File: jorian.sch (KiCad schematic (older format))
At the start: 56 parts, among them J1 Conn_01x08

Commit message: second commit
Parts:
- removed J1: Conn_01x08, kbd:connector_custom_small, symbol Connector_Generic:Conn_01x08
- added G1, G2: Logo_Open_Hardware_Small, kbd:jorian_logo, symbol Graphic:Logo_Open_Hardware_Small
- added H1: Battery Pad, kbd:battery_pad, symbol Mechanical:MountingHole_Pad
- added J2: conn_i2c, kbd:connector_i2c, symbol Connector_Generic:Conn_01x04
- added J3: conn_swd, kbd:connector_swd, symbol Connector_Generic:Conn_01x05
- added JP1: BAT+, kbd:jumper_3way, symbol Jumper:SolderJumper_3_Open
- added JP2: GND, kbd:jumper_3way, symbol Jumper:SolderJumper_3_Open
- added JP3: VCC, kbd:jumper_3way, symbol Jumper:SolderJumper_3_Open
- added JP4: SCL, kbd:jumper_3way, symbol Jumper:SolderJumper_3_Open
- added JP5: SDA, kbd:jumper_3way, symbol Jumper:SolderJumper_3_Open
- BT1: value Battery_Cell -> Battery Holder
- E10, E15, E18, E5: value edge_conn_left -> left; symbol kbd:edge_conn -> Connector_Generic:Conn_01x05
- E16, E19, E20, E21: value edge_conn_right -> right; symbol kbd:edge_conn -> Connector_Generic:Conn_01x05
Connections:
- net labels added: RX, SWC, SWD, TX
- net labels removed: SWCLK, SWDIO
- wire segments 264 -> 275
- no-connect marks 7 -> 17
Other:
- moved on the sheet: BT1

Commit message: added charger
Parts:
- removed J2: conn_i2c, kbd:connector_i2c, symbol Connector_Generic:Conn_01x04
- removed J3: conn_swd, kbd:connector_swd, symbol Connector_Generic:Conn_01x05
- removed JP1: BAT+, kbd:jumper_3way, symbol Jumper:SolderJumper_3_Open
- removed JP2: GND, kbd:jumper_3way, symbol Jumper:SolderJumper_3_Open
- removed JP3: VCC, kbd:jumper_3way, symbol Jumper:SolderJumper_3_Open
- removed JP4: SCL, kbd:jumper_3way, symbol Jumper:SolderJumper_3_Open
- removed JP5: SDA, kbd:jumper_3way, symbol Jumper:SolderJumper_3_Open
- added C3, C4: 0.1uF, kbd:C_0805, symbol Device:C
- added C5: 10uF, kbd:C_0805, symbol Device:C
- added J1, J3: MicroUSB, kbd:usb_micro_custom, symbol Connector:USB_B_Micro
- added J2, J4: USB-C, kbd:usb_type_c, symbol Connector:USB_C_Receptacle_USB2.0
- added J5: MJ-4PP-9, kbd:trrs_connector, symbol kbd:kbd_MJ-4PP-9
- added JP1: B+, kbd:jumper, symbol Device:Jumper_NO_Small
- added JP10: B-, kbd:jumper, symbol Device:Jumper_NO_Small
- added JP11, JP13: VCC, kbd:jumper, symbol Device:Jumper_NO_Small
- added JP12, JP14: GND, kbd:jumper, symbol Device:Jumper_NO_Small
- added JP15: SKIP, kbd:jumper, symbol Device:Jumper_NO_Small
- added JP2, JP3, JP4, JP5, JP6, JP7, JP8, JP9: (no value), kbd:jumper, symbol Device:Jumper_NO_Small
- added OLED1, OLED2: I2C_conn, kbd:connector_i2c, symbol Connector_Generic:Conn_01x04
- added R1: 1.2K, kbd:R_0805, symbol Device:R
- added R2: 1K, kbd:R_0805, symbol Device:R
- added R3: 100, kbd:R_0805, symbol Device:R
- added SW1: SW_SPDT, kbd:switch_MSK-12C02_smd, symbol Switch:SW_SPDT
- added SWD1: SWD_conn, kbd:connector_swd, symbol Connector_Generic:Conn_01x05
- added U3: AMS1117, kbd:SOT-223-3, symbol Regulator_Linear:AMS1117
- added U4: TP4056, kbd:SOP-8, symbol kbd:TP4056
- added U5: DW01A, kbd:SOT-23-6, symbol kbd:DW01A
- added U6: FS8205A, kbd:TSSOP-8, symbol kbd:FS8205A
- E10, E15, E18, E5: footprint kbd:edge_conn_left -> kbd:edge_conn; symbol Connector_Generic:Conn_01x05 -> Connector_Generic:Conn_01x04
- E16, E19, E20, E21: footprint kbd:edge_conn_right -> kbd:edge_conn; symbol Connector_Generic:Conn_01x05 -> Connector_Generic:Conn_01x04
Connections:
- net labels added: 3.3V, 5V, B+, B-, BAT+, D+, D-, IN+, IN-, OUT+, OUT-
- wire segments 275 -> 372
- no-connect marks 17 -> 26
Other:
- note added: "LiPo Charger"
- moved on the sheet: H1

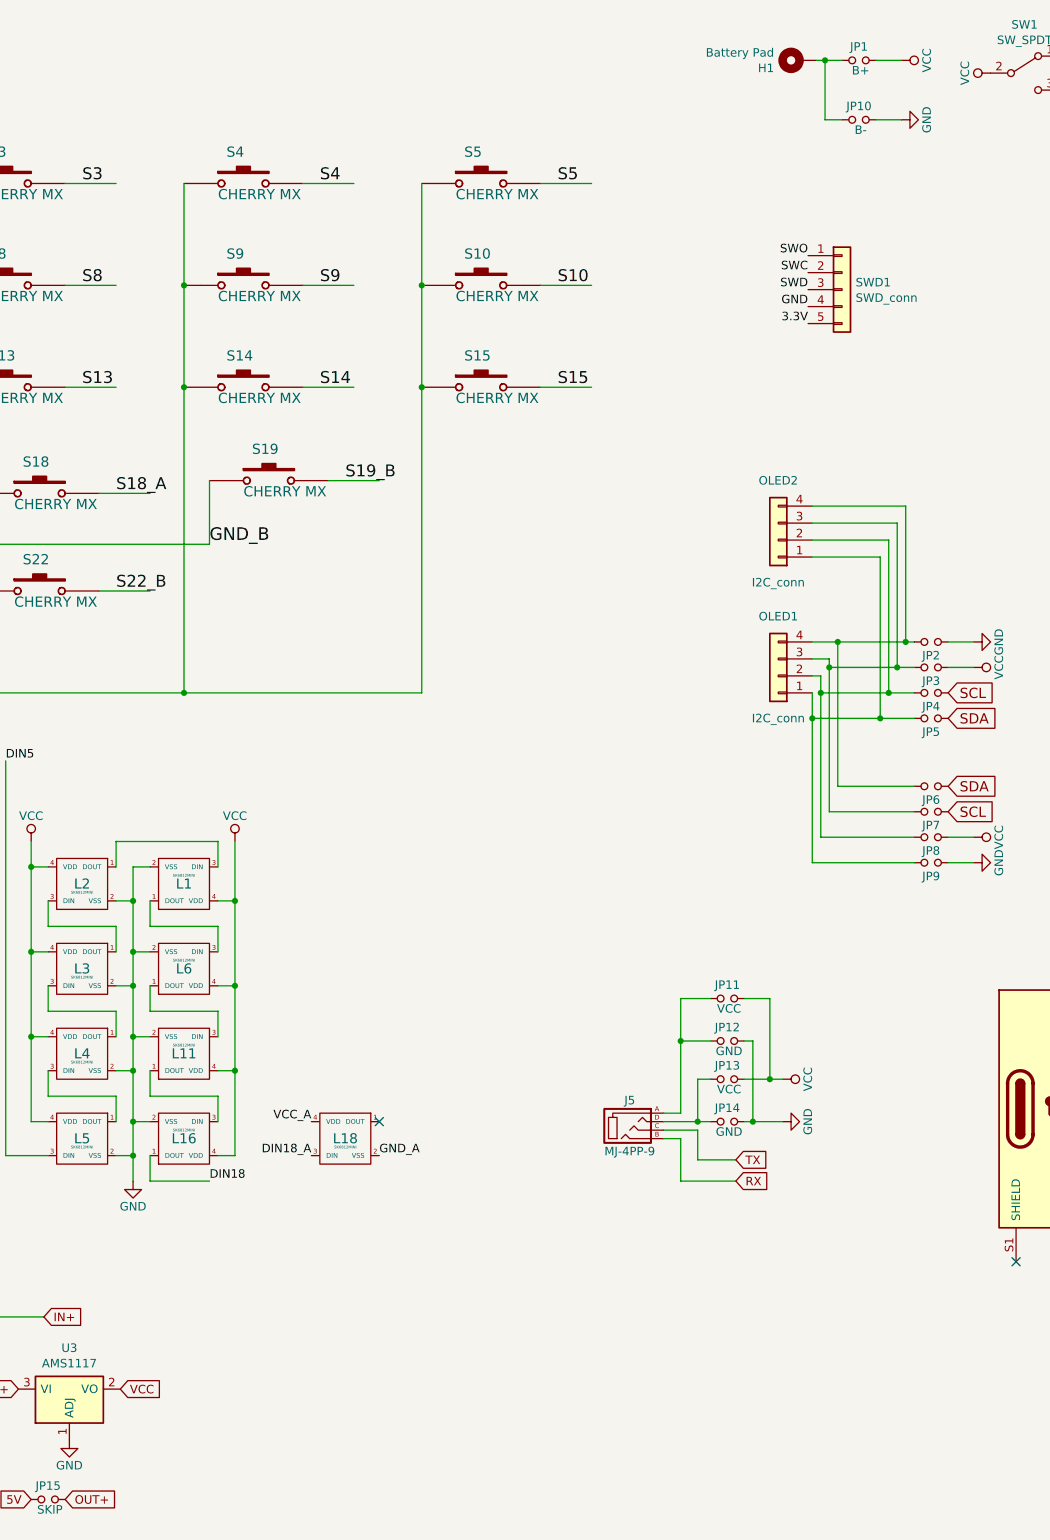
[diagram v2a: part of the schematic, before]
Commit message: autorouted charger take 1
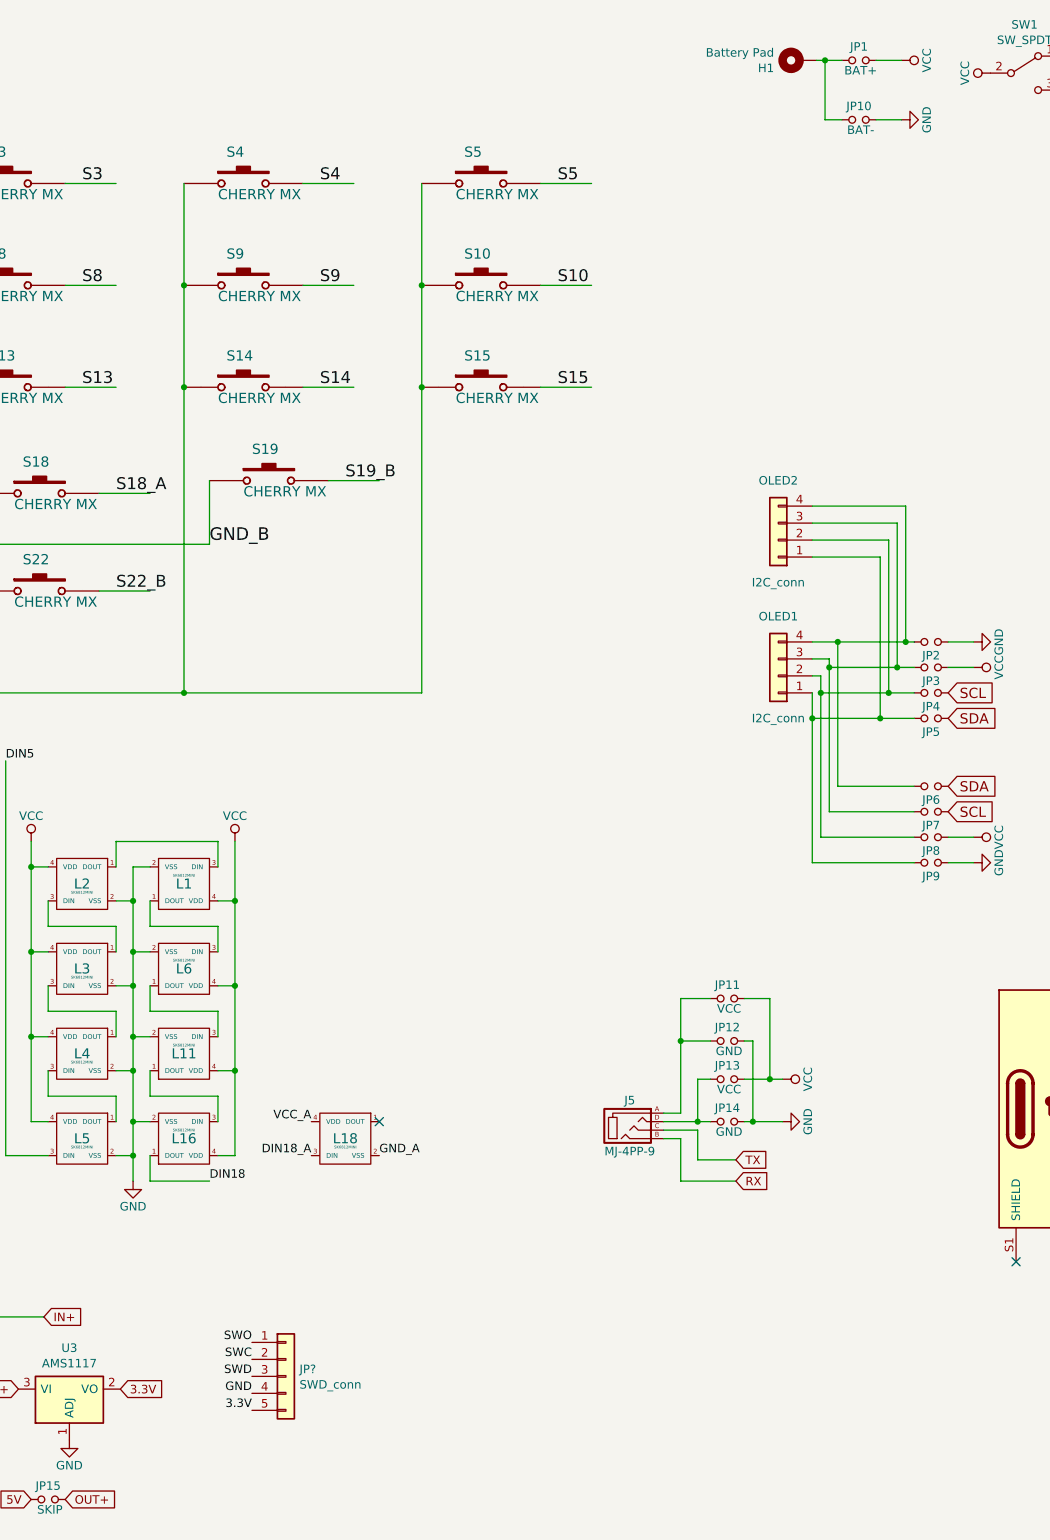
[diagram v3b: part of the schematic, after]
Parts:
- JP1: value B+ -> BAT+
- JP10: value B- -> BAT-
- renumbered SWD1 to JP?
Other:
- moved on the sheet: JP?
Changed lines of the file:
@@
 	1    0    0    -1
 $EndComp
-Text Label 12575 2175 2    50   ~ 0
+Text Label 9300 8575 2    50   ~ 0
 SWO
-Text Label 12575 2275 2    50   ~ 0
+Text Label 9300 8675 2    50   ~ 0
 SWC
-Text Label 12575 2375 2    50   ~ 0
+Text Label 9300 8775 2    50   ~ 0
 SWD
-Text Label 12575 2475 2    50   ~ 0
+Text Label 9300 8875 2    50   ~ 0
 GND
-Text Label 12575 2575 2    50   ~ 0
+Text Label 9300 8975 2    50   ~ 0
 3.3V
 Text Label 14050 1200 0    50   ~ 0
@@
 	12750 4450 13150 4450
 $Comp
-L Connector_Generic:Conn_01x05 SWD1
+L Connector_Generic:Conn_01x05 JP?
 U 1 1 5C1CF656
-P 12775 2375
-F 0 "SWD1" H 12855 2417 50  0000 L CNN
-F 1 "SWD_conn" H 12855 2326 50  0000 L CNN
-F 2 "kbd:connector_swd" H 12775 2375 50  0001 C CNN
-F 3 "~" H 12775 2375 50  0001 C CNN
-	1    12775 2375
+P 9500 8775
+F 0 "JP?" H 9580 8817 50  0000 L CNN
+F 1 "SWD_conn" H 9580 8726 50  0000 L CNN
+F 2 "kbd:connector_swd" H 9500 8775 50  0001 C CNN
+F 3 "~" H 9500 8775 50  0001 C CNN
+	1    9500 8775
 	1    0    0    -1
 $EndComp
@@
 P 12875 1025
 F 0 "JP1" H 12875 1105 50  0000 C CNN
-F 1 "B+" H 12885 965 50  0000 C CNN
+F 1 "BAT+" H 12885 965 50  0000 C CNN
 F 2 "kbd:jumper" H 12875 1025 50  0001 C CNN
 F 3 "" H 12875 1025 50  0001 C CNN
@@
 P 12875 1375
 F 0 "JP10" H 12875 1455 50  0000 C CNN
-F 1 "B-" H 12885 1315 50  0000 C CNN
+F 1 "BAT-" H 12885 1315 50  0000 C CNN
 F 2 "kbd:jumper" H 12875 1375 50  0001 C CNN
 F 3 "" H 12875 1375 50  0001 C CNN
@@
 5V
 Text GLabel 8525 8850 2    50   Input ~ 0
-VCC
+3.3V
 Text GLabel 7800 8425 0    50   Input ~ 0
 5V

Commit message: autorouted charger take 2
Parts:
- JP1: value BAT+ -> B+
- JP10: value BAT- -> B-
- gave numbers to parts that had none: 1
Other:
- moved on the sheet: BT1, H1, JP1, JP10, JP15, JP16, SW1
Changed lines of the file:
@@
 L Device:Battery_Cell BT1
 U 1 1 5C194810
-P 14725 1075
-F 0 "BT1" H 14843 1171 50  0000 L CNN
-F 1 "Battery Holder" H 14843 1080 50  0000 L CNN
-F 2 "kbd:cr2032_bs-7" V 14725 1135 50  0001 C CNN
-F 3 "~" V 14725 1135 50  0001 C CNN
-	1    14725 1075
+P 9400 8850
+F 0 "BT1" H 9518 8946 50  0000 L CNN
+F 1 "Battery Holder" H 9518 8855 50  0000 L CNN
+F 2 "kbd:cr2032_bs-7" V 9400 8910 50  0001 C CNN
+F 3 "~" V 9400 8910 50  0001 C CNN
+	1    9400 8850
 	1    0    0    -1
 $EndComp
@@
 Wire Wire Line
 	2850 2300 3150 2300
-Text Label 14725 875  0    50   ~ 0
+Text Label 9400 8650 0    50   ~ 0
 BAT+
-Text Label 14725 1175 0    50   ~ 0
+Text Label 9400 8950 0    50   ~ 0
 GND
 Text Label 1250 1300 2    70   ~ 0
@@
 L Mechanical:MountingHole_Pad H1
 U 1 1 5C36F98B
-P 12525 1025
-F 0 "H1" V 12479 1175 50  0000 L CNN
-F 1 "Battery Pad" V 12570 1175 50  0000 L CNN
-F 2 "kbd:battery_pad" H 12525 1025 50  0001 C CNN
-F 3 "~" H 12525 1025 50  0001 C CNN
-	1    12525 1025
+P 9725 9400
+F 0 "H1" V 9679 9550 50  0000 L CNN
+F 1 "Battery Pad" V 9770 9550 50  0000 L CNN
+F 2 "kbd:battery_pad" H 9725 9400 50  0001 C CNN
+F 3 "~" H 9725 9400 50  0001 C CNN
+	1    9725 9400
 	0    -1   -1   0
 $EndComp
@@
 L Switch:SW_SPDT SW1
 U 1 1 5CD134D6
-P 13850 1100
-F 0 "SW1" H 13850 1385 50  0000 C CNN
-F 1 "SW_SPDT" H 13850 1294 50  0000 C CNN
-F 2 "kbd:switch_MSK-12C02_smd" H 13850 1100 50  0001 C CNN
-F 3 "" H 13850 1100 50  0001 C CNN
-	1    13850 1100
-	1    0    0    -1
-$EndComp
-Text Label 9300 8575 2    50   ~ 0
+P 10675 8875
+F 0 "SW1" H 10675 9160 50  0000 C CNN
+F 1 "SW_SPDT" H 10675 9069 50  0000 C CNN
+F 2 "kbd:switch_MSK-12C02_smd" H 10675 8875 50  0001 C CNN
+F 3 "" H 10675 8875 50  0001 C CNN
+	1    10675 8875
+	1    0    0    -1
+$EndComp
+Text Label 12650 2550 2    50   ~ 0
 SWO
-Text Label 9300 8675 2    50   ~ 0
+Text Label 12650 2650 2    50   ~ 0
 SWC
-Text Label 9300 8775 2    50   ~ 0
+Text Label 12650 2750 2    50   ~ 0
 SWD
-Text Label 9300 8875 2    50   ~ 0
+Text Label 12650 2850 2    50   ~ 0
 GND
-Text Label 9300 8975 2    50   ~ 0
+Text Label 12650 2950 2    50   ~ 0
 3.3V
-Text Label 14050 1200 0    50   ~ 0
+Text Label 10875 8975 0    50   ~ 0
 BAT+
-Text Label 14050 1000 0    50   ~ 0
+Text Label 10875 8775 0    50   ~ 0
 3.3V
 Text Label 14700 6600 0    50   ~ 0
@@
 	12750 4450 13150 4450
 $Comp
-L Connector_Generic:Conn_01x05 JP?
+L Connector_Generic:Conn_01x05 JP16
 U 1 1 5C1CF656
-P 9500 8775
-F 0 "JP?" H 9580 8817 50  0000 L CNN
-F 1 "SWD_conn" H 9580 8726 50  0000 L CNN
-F 2 "kbd:connector_swd" H 9500 8775 50  0001 C CNN
-F 3 "~" H 9500 8775 50  0001 C CNN
-	1    9500 8775
+P 12850 2750
+F 0 "JP16" H 12930 2792 50  0000 L CNN
+F 1 "SWD_conn" H 12930 2701 50  0000 L CNN
+F 2 "kbd:connector_swd" H 12850 2750 50  0001 C CNN
+F 3 "~" H 12850 2750 50  0001 C CNN
+	1    12850 2750
 	1    0    0    -1
 $EndComp
@@
 L Device:Jumper_NO_Small JP1
 U 1 1 5C4D6698
-P 12875 1025
-F 0 "JP1" H 12875 1105 50  0000 C CNN
-F 1 "BAT+" H 12885 965 50  0000 C CNN
-F 2 "kbd:jumper" H 12875 1025 50  0001 C CNN
-F 3 "" H 12875 1025 50  0001 C CNN
-	1    12875 1025
+P 10075 9400
+F 0 "JP1" H 10075 9480 50  0000 C CNN
+F 1 "B+" H 10085 9340 50  0000 C CNN
+F 2 "kbd:jumper" H 10075 9400 50  0001 C CNN
+F 3 "" H 10075 9400 50  0001 C CNN
+	1    10075 9400
 	1    0    0    -1
 $EndComp
@@
 L Device:Jumper_NO_Small JP10
 U 1 1 5C4D669F
-P 12875 1375
-F 0 "JP10" H 12875 1455 50  0000 C CNN
-F 1 "BAT-" H 12885 1315 50  0000 C CNN
-F 2 "kbd:jumper" H 12875 1375 50  0001 C CNN
-F 3 "" H 12875 1375 50  0001 C CNN
-	1    12875 1375
+P 10075 9750
+F 0 "JP10" H 10075 9830 50  0000 C CNN
+F 1 "B-" H 10085 9690 50  0000 C CNN
+F 2 "kbd:jumper" H 10075 9750 50  0001 C CNN
+F 3 "" H 10075 9750 50  0001 C CNN
+	1    10075 9750
 	1    0    0    -1
 $EndComp
@@
 L power:GND #PWR0125
 U 1 1 5C4D66A6
-P 13125 1375
-F 0 "#PWR0125" H 13125 1125 50  0001 C CNN
-F 1 "GND" H 13125 1225 50  0000 C CNN
-F 2 "" H 13125 1375 50  0001 C CNN
-F 3 "" H 13125 1375 50  0001 C CNN
-	1    13125 1375
+P 10325 9750
+F 0 "#PWR0125" H 10325 9500 50  0001 C CNN
+F 1 "GND" H 10325 9600 50  0000 C CNN
+F 2 "" H 10325 9750 50  0001 C CNN
+F 3 "" H 10325 9750 50  0001 C CNN
+	1    10325 9750
 	0    -1   -1   0
 $EndComp
@@
 L power:VCC #PWR0126
 U 1 1 5C4D66AC
-P 13125 1025
-F 0 "#PWR0126" H 13125 875 50  0001 C CNN
-F 1 "VCC" H 13125 1175 50  0000 C CNN
-F 2 "" H 13125 1025 50  0001 C CNN
-F 3 "" H 13125 1025 50  0001 C CNN
-	1    13125 1025
+P 10325 9400
+F 0 "#PWR0126" H 10325 9250 50  0001 C CNN
+F 1 "VCC" H 10325 9550 50  0000 C CNN
+F 2 "" H 10325 9400 50  0001 C CNN
+F 3 "" H 10325 9400 50  0001 C CNN
+	1    10325 9400
 	0    1    1    0
 $EndComp
 Wire Wire Line
-	12975 1375 13125 1375
-Wire Wire Line
-	12975 1025 13125 1025
-Wire Wire Line
-	12775 1025 12675 1025
-Wire Wire Line
-	12775 1375 12675 1375
-Wire Wire Line
-	12675 1375 12675 1025
-Connection ~ 12675 1025
-Wire Wire Line
-	12675 1025 12625 1025
+	10175 9750 10325 9750
+Wire Wire Line
+	10175 9400 10325 9400
+Wire Wire Line
+	9975 9400 9875 9400
+Wire Wire Line
+	9975 9750 9875 9750
+Wire Wire Line
+	9875 9750 9875 9400
+Connection ~ 9875 9400
+Wire Wire Line
+	9875 9400 9825 9400
 Text GLabel 12150 7500 2    50   Input ~ 0
 TX
@@
 L power:VCC #PWR0127
 U 1 1 5E714A3D
-P 13650 1100
-F 0 "#PWR0127" H 13650 950 50  0001 C CNN
-F 1 "VCC" H 13650 1250 50  0000 C CNN
-F 2 "" H 13650 1100 50  0001 C CNN
-F 3 "" H 13650 1100 50  0001 C CNN
-	1    13650 1100
+P 10475 8875
+F 0 "#PWR0127" H 10475 8725 50  0001 C CNN
+F 1 "VCC" H 10475 9025 50  0000 C CNN
+F 2 "" H 10475 8875 50  0001 C CNN
+F 3 "" H 10475 8875 50  0001 C CNN
+	1    10475 8875
 	0    -1   -1   0
 $EndComp
@@
 	1    0    0    -1
 $EndComp
-Text GLabel 8000 9500 0    50   Input ~ 0
+Text GLabel 7950 9700 0    50   Input ~ 0
 5V
 Text GLabel 8525 8850 2    50   Input ~ 0
@@
 L Device:Jumper_NO_Small JP15
 U 1 1 5C2BFB5C
-P 8100 9500
-F 0 "JP15" H 8100 9580 50  0000 C CNN
-F 1 "SKIP" H 8110 9440 50  0000 C CNN
-F 2 "kbd:jumper" H 8100 9500 50  0001 C CNN
-F 3 "" H 8100 9500 50  0001 C CNN
-	1    8100 9500
+P 8050 9700
+F 0 "JP15" H 8050 9780 50  0000 C CNN
+F 1 "SKIP" H 8060 9640 50  0000 C CNN
+F 2 "kbd:jumper" H 8050 9700 50  0001 C CNN
+F 3 "" H 8050 9700 50  0001 C CNN
+	1    8050 9700
 	1    0    0    -1
 $EndComp
@@
 Wire Wire Line
 	7800 8425 8075 8425
-Text GLabel 8200 9500 2    50   Input ~ 0
+Text GLabel 8150 9700 2    50   Input ~ 0
 OUT+
 $EndSCHEMATC

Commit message: autorouted version with better usb-c
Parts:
- J2, J4: symbol Connector:USB_C_Receptacle_USB2.0 -> jorian-rescue:USB_C_Receptacle_USB2.0-Connector
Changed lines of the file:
@@
 EESchema Schematic File Version 4
 LIBS:jorian-cache
-EELAYER 26 0
+EELAYER 29 0
 EELAYER END
 $Descr B 17000 11000
@@
 5V
 $Comp
-L Connector:USB_C_Receptacle_USB2.0 J2
+L jorian-rescue:USB_C_Receptacle_USB2.0-Connector J2
 U 1 1 5CBEE4AC
 P 14100 7200
@@
 $EndComp
 $Comp
-L Connector:USB_C_Receptacle_USB2.0 J4
+L jorian-rescue:USB_C_Receptacle_USB2.0-Connector J4
 U 1 1 5D04D0D8
 P 15550 7200

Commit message: autorouted charger, alpha version
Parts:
- added JP17: VUSB, kbd:jumper, symbol Device:Jumper_NO_Small
- added JP18: LIR+, kbd:jumper, symbol Device:Jumper_NO_Small
- added JP19: LIR-, kbd:jumper, symbol Device:Jumper_NO_Small
- added JP20: CR+, kbd:jumper, symbol Device:Jumper_NO_Small
- added JP21: CR-, kbd:jumper, symbol Device:Jumper_NO_Small
- added JP22: D+, kbd:jumper, symbol Device:Jumper_NO_Small
- added JP23: D-, kbd:jumper, symbol Device:Jumper_NO_Small
- added JP24: TX, kbd:jumper, symbol Device:Jumper_NO_Small
- added JP25: RX, kbd:jumper, symbol Device:Jumper_NO_Small
- added R4, R5: 1.5K, kbd:R_0805, symbol Device:R
- JP1: value B+ -> BAT+
- JP10: value B- -> BAT-
- JP15: value SKIP -> VUSB
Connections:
- net labels added: BAT-, LIPO+, LIPO-, VUSB
- net labels removed: 5V, B+, B-, IN+, IN-
- wire segments 372 -> 403
- no-connect marks 26 -> 25
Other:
- moved on the sheet: BT1, H1, J5, JP1, JP10, JP15, JP16, JP2, JP3, JP4, JP5, JP6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
